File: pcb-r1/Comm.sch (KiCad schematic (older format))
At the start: 12 parts

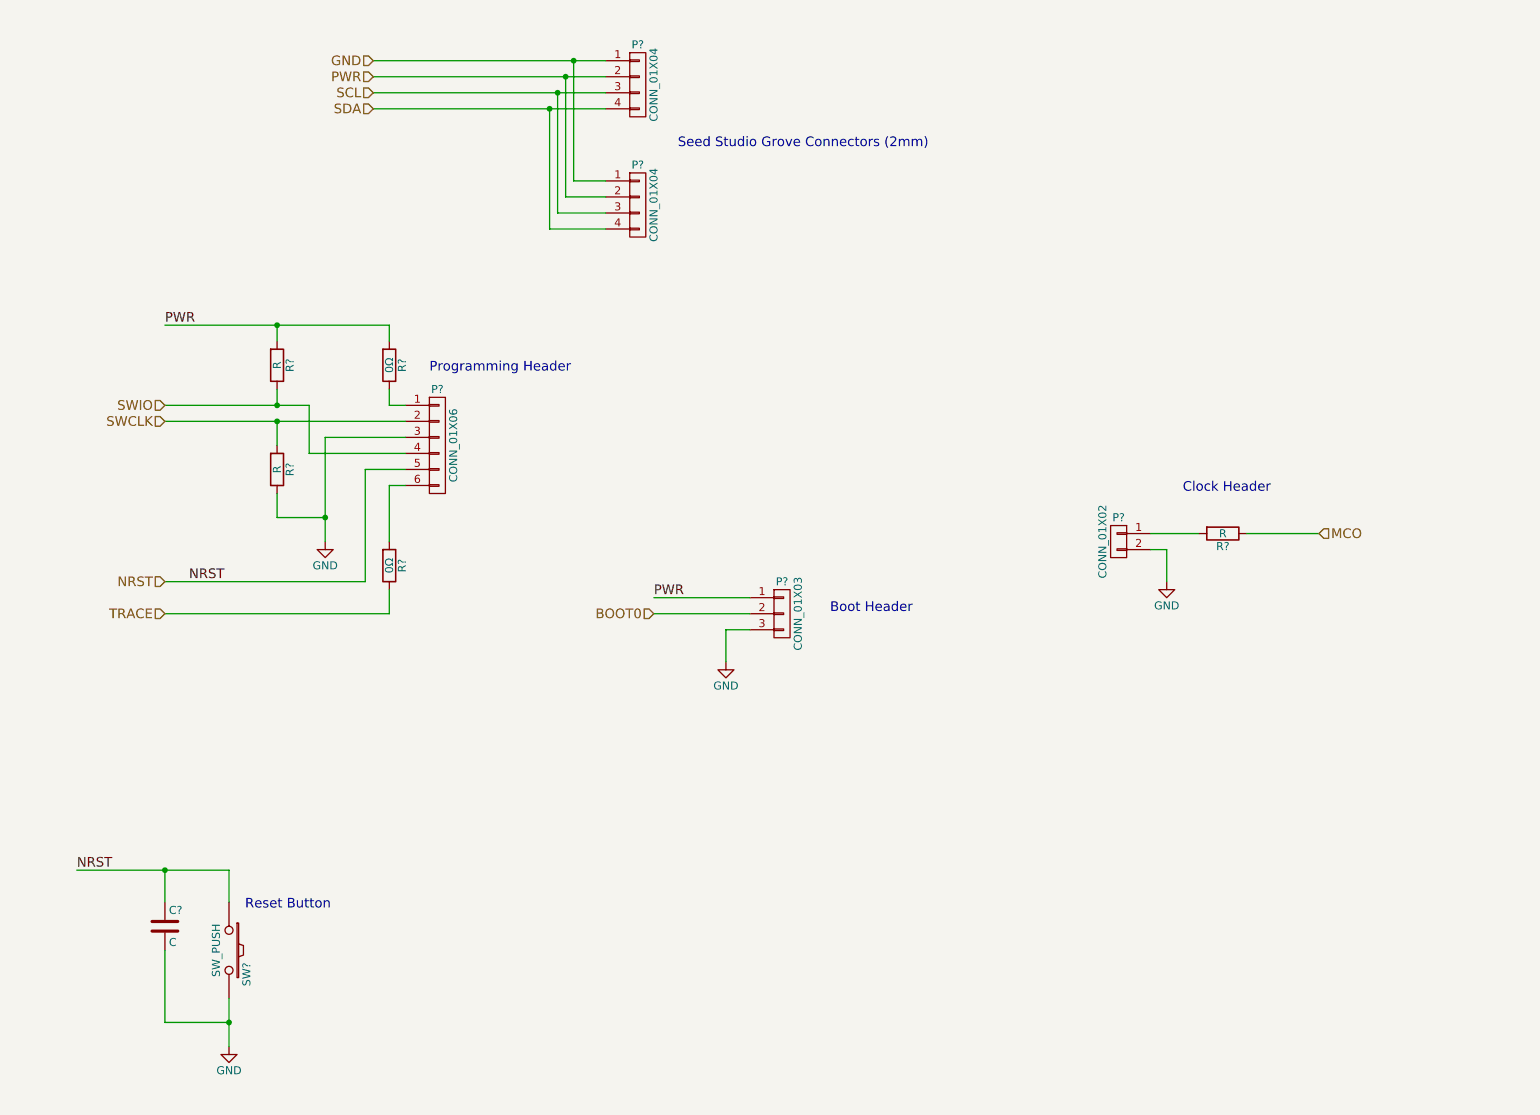
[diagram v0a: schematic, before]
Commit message: Edited the Central-Command.sch and forced the order of the hierarchical sheets to match the reference schematic annotations. Also annotated
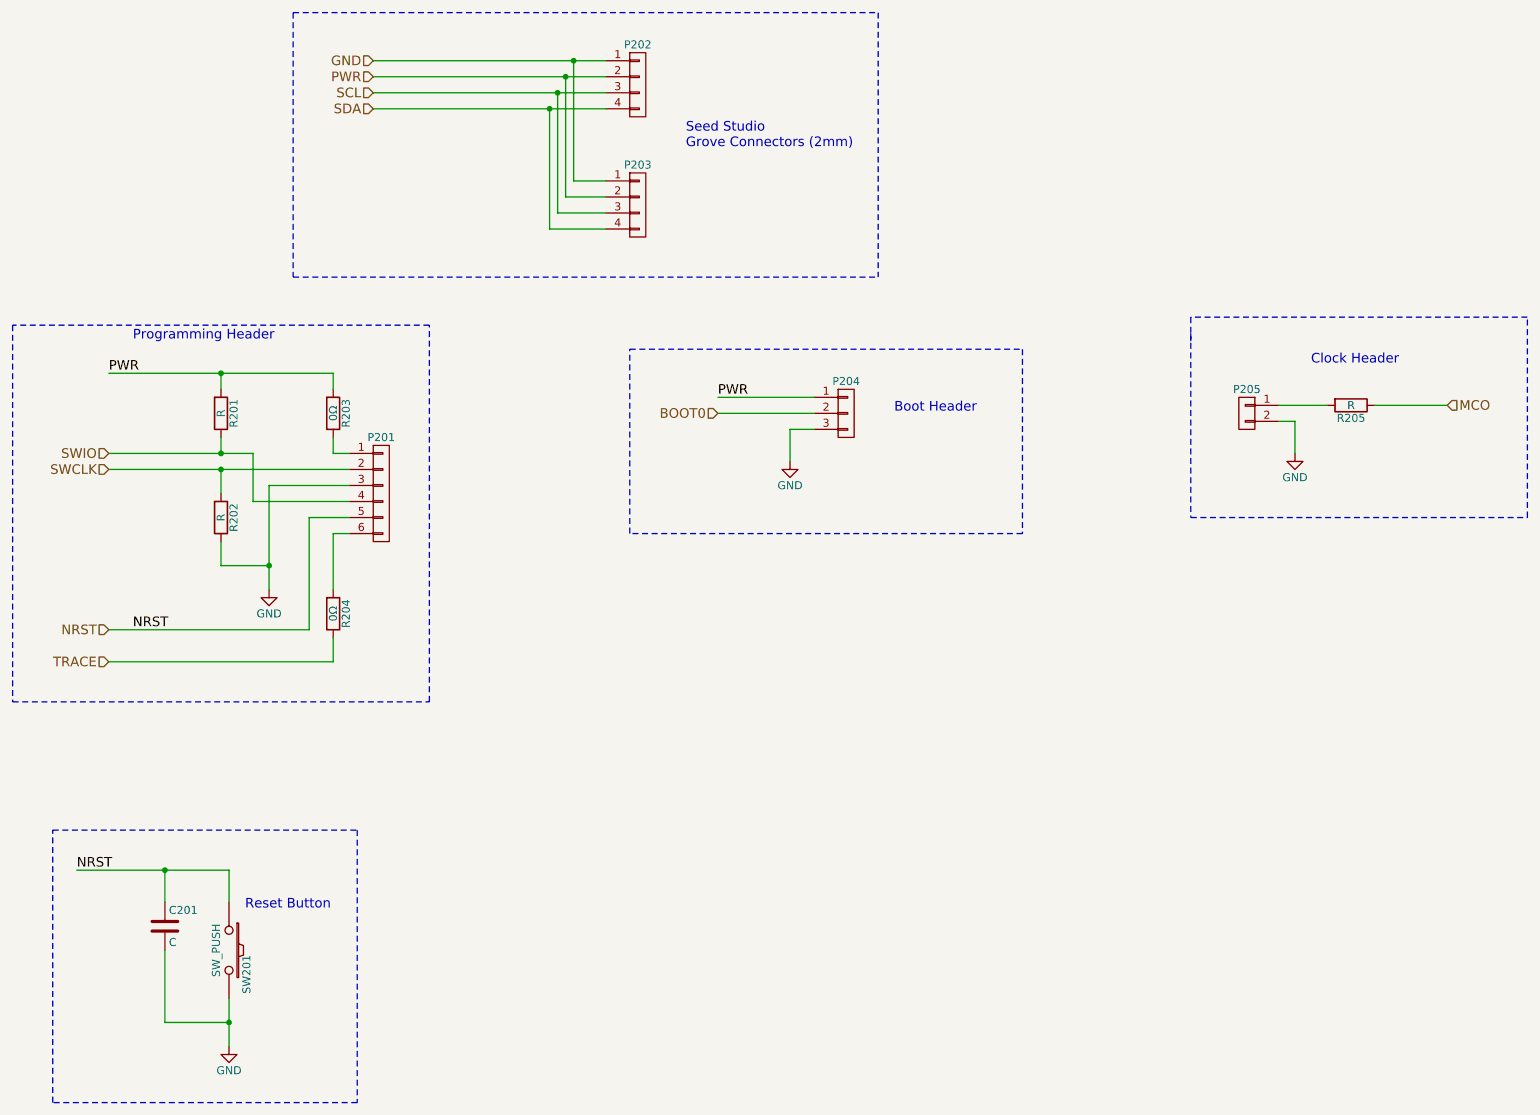
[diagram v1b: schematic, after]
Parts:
- gave numbers to parts that had none: 12
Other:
- note added: "Seed Studio \nGrove Connectors (2mm)"
- note removed: "Seed Studio Grove Connectors (2mm)"
- moved on the sheet: P201, P204, P205, R201, R202, R203, R204, R205

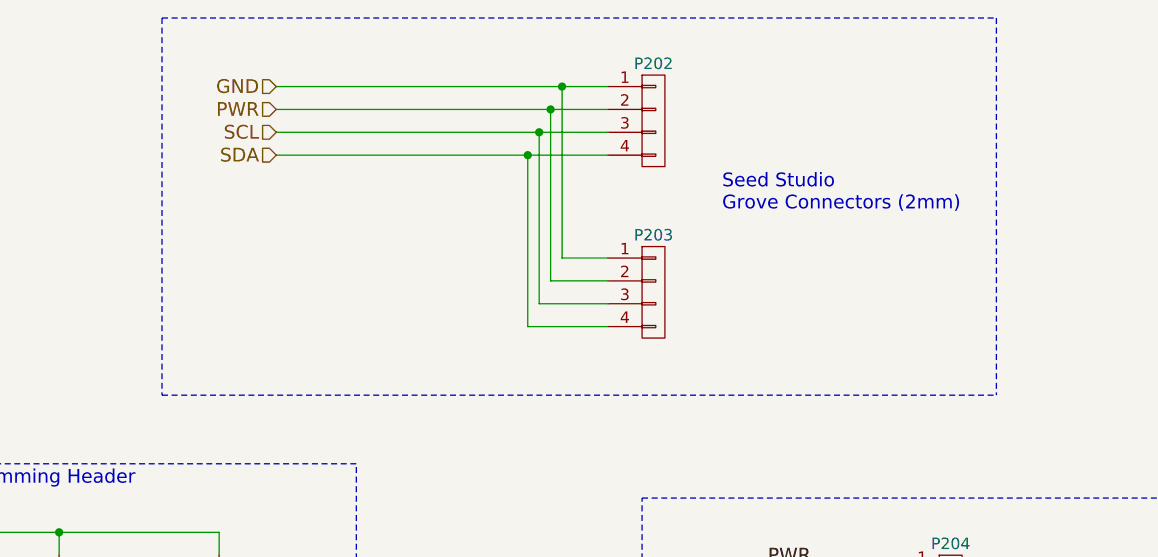
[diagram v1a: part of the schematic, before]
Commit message: Started the part to footprint association
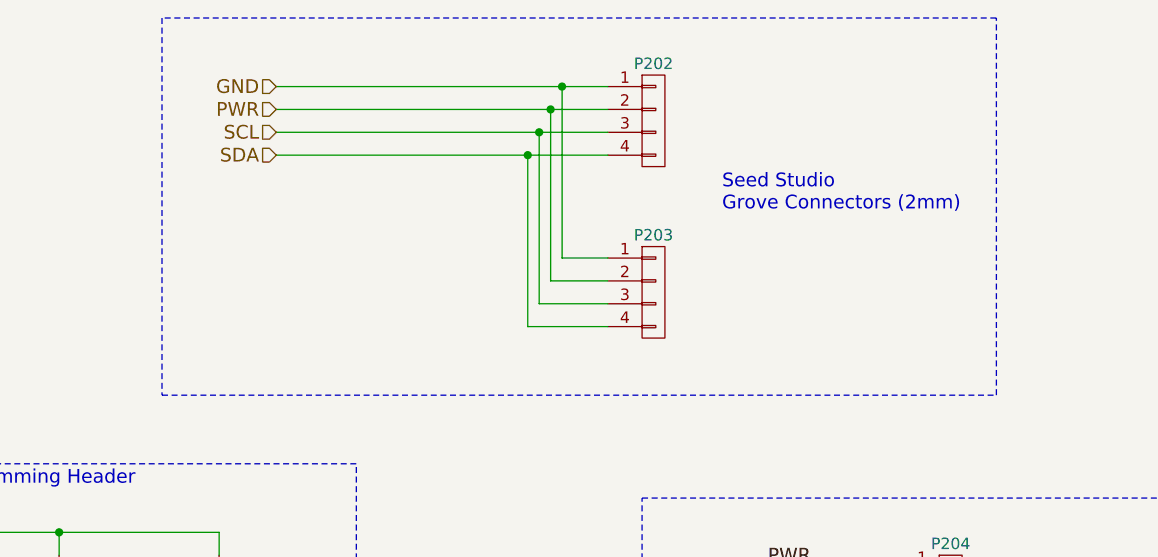
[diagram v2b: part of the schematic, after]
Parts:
- P202, P203: footprint (none) -> CentralCommand:Grove-2mm
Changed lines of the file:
@@
 F 0 "C201" H 1975 6550 50  0000 L CNN
 F 1 "C" H 1975 6350 50  0000 L CNN
-F 2 "" H 1988 6300 30  0000 C CNN
+F 2 "" H 1988 6300 30  0001 C CNN
 F 3 "" H 1950 6450 60  0000 C CNN
 	1    1950 6450
@@
 F 0 "SW201" H 2500 6710 50  0000 C CNN
 F 1 "SW_PUSH" H 2350 6520 50  0000 C CNN
-F 2 "" H 2350 6600 60  0000 C CNN
+F 2 "" H 2350 6600 60  0001 C CNN
 F 3 "" H 2350 6600 60  0000 C CNN
 	1    2350 6600
@@
 $EndComp
 $Comp
-L GND #PWR201
+L GND #PWR06
 U 1 1 56673C8A
 P 2350 7200
-F 0 "#PWR201" H 2350 6950 50  0001 C CNN
+F 0 "#PWR06" H 2350 6950 50  0001 C CNN
 F 1 "GND" H 2350 7050 50  0000 C CNN
 F 2 "" H 2350 7200 60  0000 C CNN
@@
 $EndComp
 $Comp
-L GND #PWR202
+L GND #PWR07
 U 1 1 56674184
 P 2600 4350
-F 0 "#PWR202" H 2600 4100 50  0001 C CNN
+F 0 "#PWR07" H 2600 4100 50  0001 C CNN
 F 1 "GND" H 2600 4200 50  0000 C CNN
 F 2 "" H 2600 4350 60  0000 C CNN
@@
 F 0 "P202" H 4900 1450 50  0000 C CNN
 F 1 "CONN_01X04" V 5000 1200 50  0001 C CNN
-F 2 "" H 4900 1200 60  0000 C CNN
+F 2 "CentralCommand:Grove-2mm" H 4900 1200 60  0001 C CNN
 F 3 "" H 4900 1200 60  0000 C CNN
 	1    4900 1200
@@
 F 0 "P203" H 4900 2200 50  0000 C CNN
 F 1 "CONN_01X04" V 5000 1950 50  0001 C CNN
-F 2 "" H 4900 1950 60  0000 C CNN
+F 2 "CentralCommand:Grove-2mm" H 4900 1950 60  0001 C CNN
 F 3 "" H 4900 1950 60  0000 C CNN
 	1    4900 1950
@@
 F 0 "P204" H 6200 3450 50  0000 C CNN
 F 1 "CONN_01X03" V 6300 3250 50  0001 C CNN
-F 2 "" H 6200 3250 60  0000 C CNN
+F 2 "" H 6200 3250 60  0001 C CNN
 F 3 "" H 6200 3250 60  0000 C CNN
 	1    6200 3250
@@
 PWR
 $Comp
-L GND #PWR203
+L GND #PWR08
 U 1 1 56674C0D
 P 5850 3550
-F 0 "#PWR203" H 5850 3300 50  0001 C CNN
+F 0 "#PWR08" H 5850 3300 50  0001 C CNN
 F 1 "GND" H 5850 3400 50  0000 C CNN
 F 2 "" H 5850 3550 60  0000 C CNN
@@
 F 0 "P205" H 8700 3400 50  0000 C CNN
 F 1 "CONN_01X02" V 8800 3250 50  0001 C CNN
-F 2 "" H 8700 3250 60  0000 C CNN
+F 2 "" H 8700 3250 60  0001 C CNN
 F 3 "" H 8700 3250 60  0000 C CNN
 	1    8700 3250
@@
 F 0 "R205" V 9430 3200 50  0000 C CNN
 F 1 "R" V 9350 3200 50  0000 C CNN
-F 2 "" V 9280 3200 30  0000 C CNN
+F 2 "" V 9280 3200 30  0001 C CNN
 F 3 "" H 9350 3200 30  0000 C CNN
 	1    9350 3200
@@
 	8900 3200 9200 3200
 $Comp
-L GND #PWR204
+L GND #PWR09
 U 1 1 56674E8A
 P 9000 3500
-F 0 "#PWR204" H 9000 3250 50  0001 C CNN
+F 0 "#PWR09" H 9000 3250 50  0001 C CNN
 F 1 "GND" H 9000 3350 50  0000 C CNN
 F 2 "" H 9000 3500 60  0000 C CNN
@@
 	2750 2400 6400 2400
 Wire Notes Line
-	6400 750  6400 2400
-Wire Notes Line
-	2750 750  6400 750
+	6400 2400 6400 750
+Wire Notes Line
+	6400 750  2750 750
 Wire Notes Line
 	1000 2700 1000 5050

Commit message: Started preliminary layout of the parts
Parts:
- C201: footprint (none) -> Capacitors_SMD:C_0805
- P204: footprint (none) -> Pin_Headers:Pin_Header_Straight_1x03
- P205: footprint (none) -> Pin_Headers:Pin_Header_Straight_1x02
- R205: footprint (none) -> Resistors_SMD:R_0805
- SW201: footprint (none) -> CentralCommand:PTS525SM15SMTR2LFS
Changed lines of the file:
@@
 F 0 "C201" H 1975 6550 50  0000 L CNN
 F 1 "C" H 1975 6350 50  0000 L CNN
-F 2 "" H 1988 6300 30  0001 C CNN
+F 2 "Capacitors_SMD:C_0805" H 1988 6300 30  0001 C CNN
 F 3 "" H 1950 6450 60  0000 C CNN
 	1    1950 6450
@@
 F 0 "SW201" H 2500 6710 50  0000 C CNN
 F 1 "SW_PUSH" H 2350 6520 50  0000 C CNN
-F 2 "" H 2350 6600 60  0001 C CNN
+F 2 "CentralCommand:PTS525SM15SMTR2LFS" H 2350 6600 60  0001 C CNN
 F 3 "" H 2350 6600 60  0000 C CNN
 	1    2350 6600
@@
 F 0 "P204" H 6200 3450 50  0000 C CNN
 F 1 "CONN_01X03" V 6300 3250 50  0001 C CNN
-F 2 "" H 6200 3250 60  0001 C CNN
+F 2 "Pin_Headers:Pin_Header_Straight_1x03" H 6200 3250 60  0001 C CNN
 F 3 "" H 6200 3250 60  0000 C CNN
 	1    6200 3250
@@
 F 0 "P205" H 8700 3400 50  0000 C CNN
 F 1 "CONN_01X02" V 8800 3250 50  0001 C CNN
-F 2 "" H 8700 3250 60  0001 C CNN
+F 2 "Pin_Headers:Pin_Header_Straight_1x02" H 8700 3250 60  0001 C CNN
 F 3 "" H 8700 3250 60  0000 C CNN
 	1    8700 3250
@@
 F 0 "R205" V 9430 3200 50  0000 C CNN
 F 1 "R" V 9350 3200 50  0000 C CNN
-F 2 "" V 9280 3200 30  0001 C CNN
+F 2 "Resistors_SMD:R_0805" V 9280 3200 30  0001 C CNN
 F 3 "" H 9350 3200 30  0000 C CNN
 	1    9350 3200

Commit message: New initial layout
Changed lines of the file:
@@
 Wire Notes Line
 	1250 7550 1250 5850
+Text Label 3500 1150 0    60   ~ 0
+PWR
 $EndSCHEMATC
